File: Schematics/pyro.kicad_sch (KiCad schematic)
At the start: 6 parts, among them J6 Pyro, Q2 BSC098N10NS5

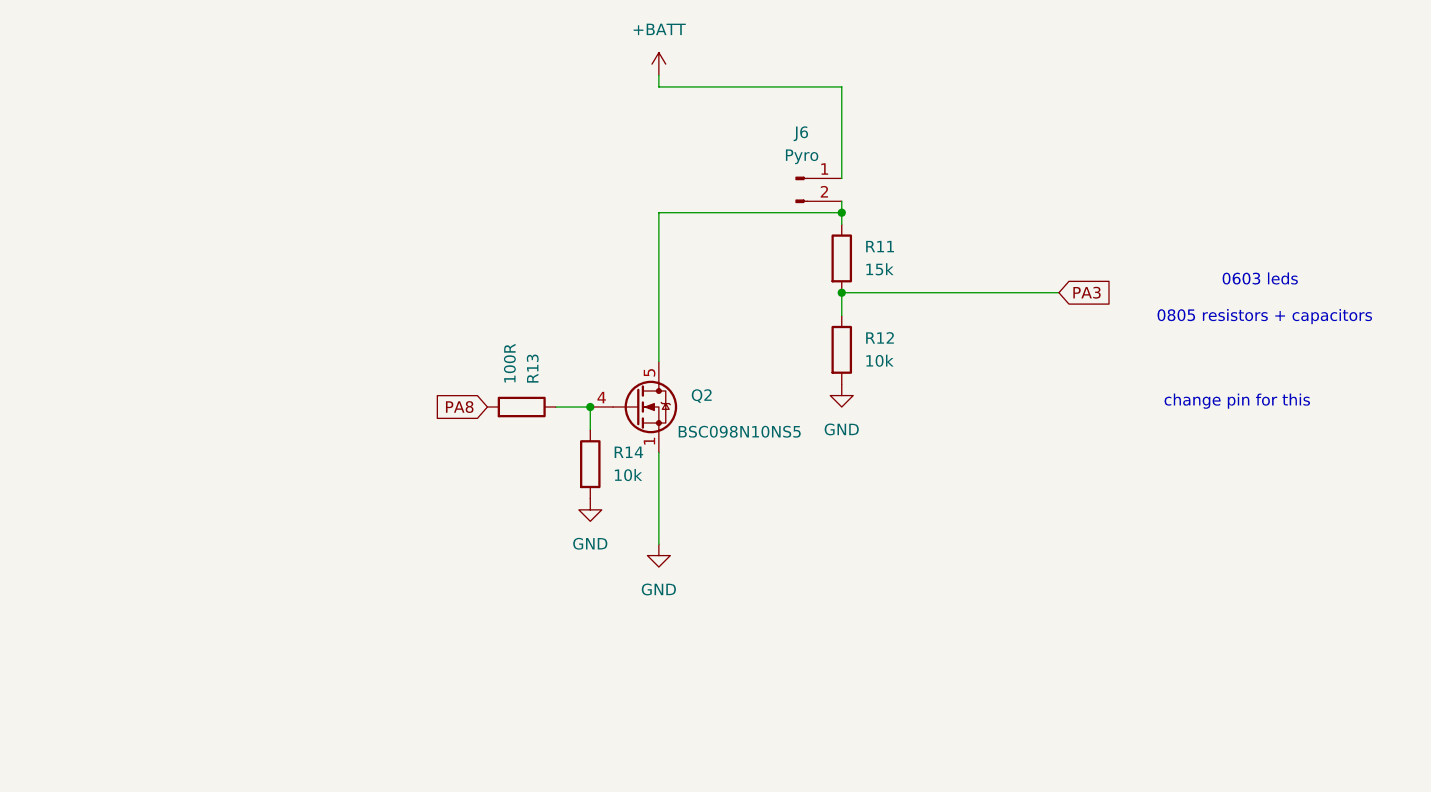
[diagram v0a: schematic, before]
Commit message: finished sensor schematics, added datasheets organized files
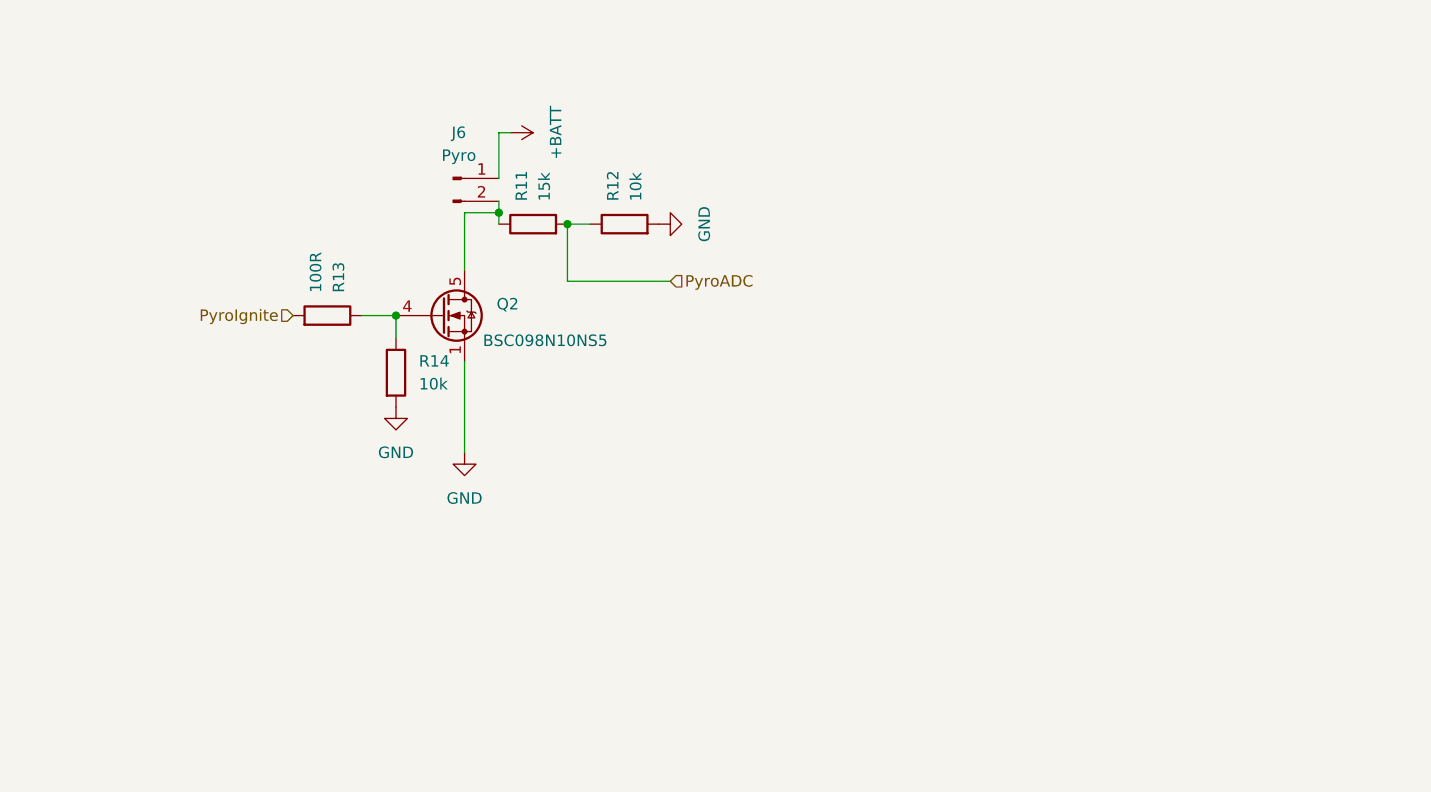
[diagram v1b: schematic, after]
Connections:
- net PA3 renamed PyroADC
- net PA8 renamed PyroIgnite
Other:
- note removed: "0603 leds"
- note removed: "0805 resistors + capacitors"
- note removed: "change pin for this"
- moved on the sheet: J6, Q2, R11, R12, R13, R14

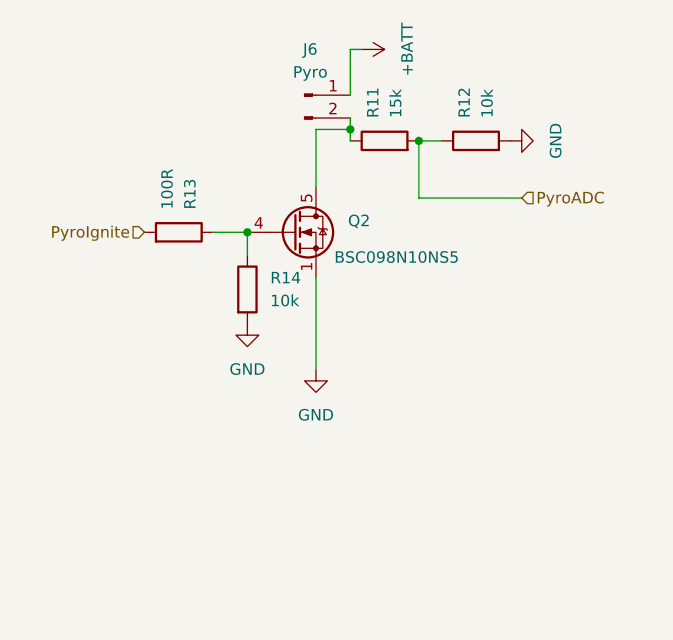
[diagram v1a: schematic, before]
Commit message: added LCSC numbers and footprint values, need to connect schemeatic pins, then can start layout
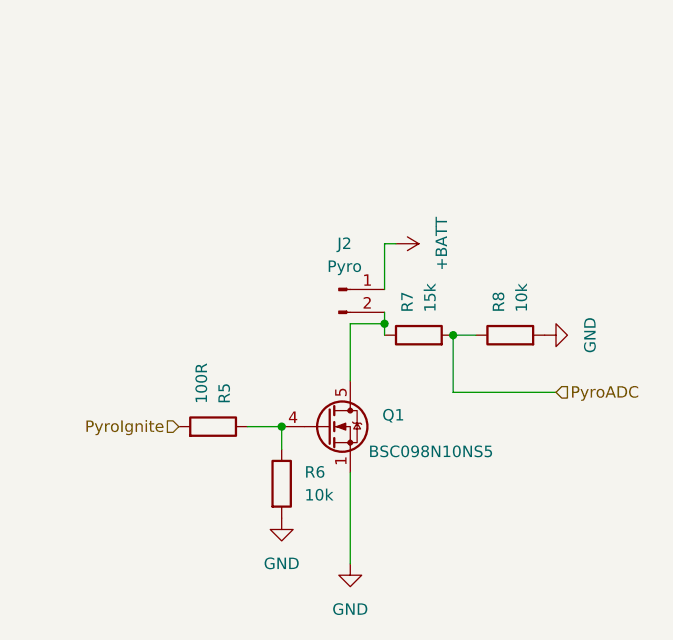
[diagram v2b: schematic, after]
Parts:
- J2: renamed from J6; footprint Connector_Molex:Molex_KK-254_AE-6410-02A_1x02_P2.54mm_Vertical -> myFootprints:MOLEX_26013114; LCSC Part (none) -> C17644051
- Q1: renamed from Q2; LCSC Part (none) -> C534398
- R5: renamed from R13; LCSC Part (none) -> C17408
- R6: renamed from R14; LCSC Part (none) -> C84376
- R7: renamed from R11; footprint Resistor_SMD:R_0805_2012Metric -> Resistor_SMD:R_0805_2012Metric_Pad1.20x1.40mm_HandSolder; LCSC Part (none) -> C2930170
- R8: renamed from R12; LCSC Part (none) -> C84376
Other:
- moved on the sheet: J2, Q1, R5, R6, R7, R8

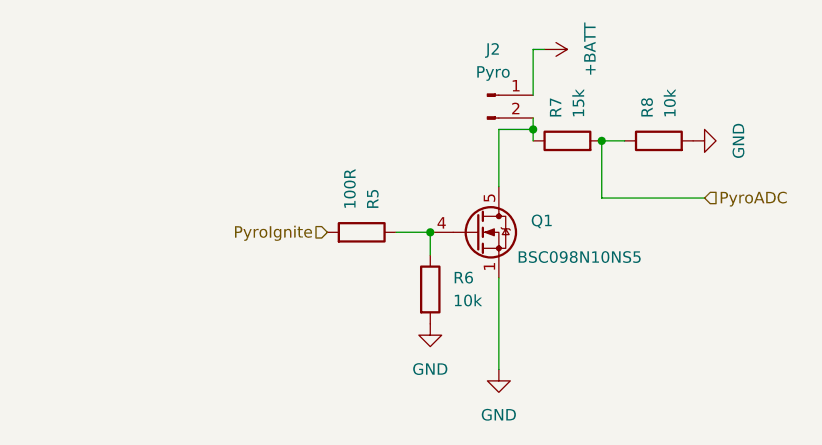
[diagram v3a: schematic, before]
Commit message: fixed symbols and added diodes to power input before ldo
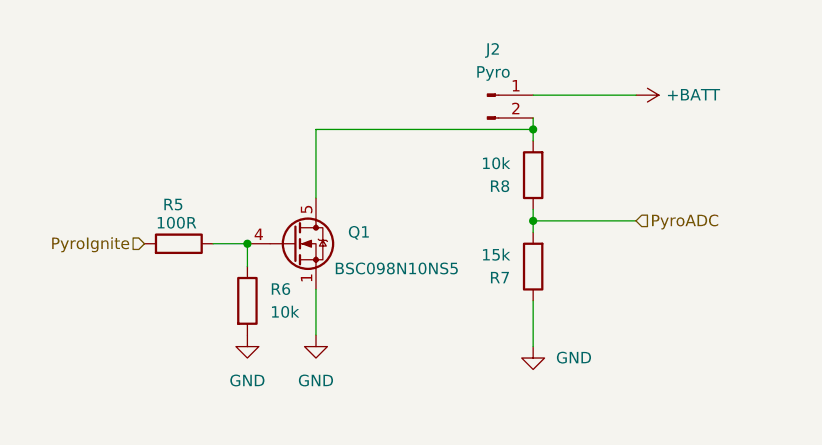
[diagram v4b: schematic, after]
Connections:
- net GND: now also R7.1; no longer R8.2
- net at J2.2 (Pin_2), Q1.5 (D): now also R8.2; no longer R7.1
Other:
- moved on the sheet: Q1, R5, R6, R7, R8

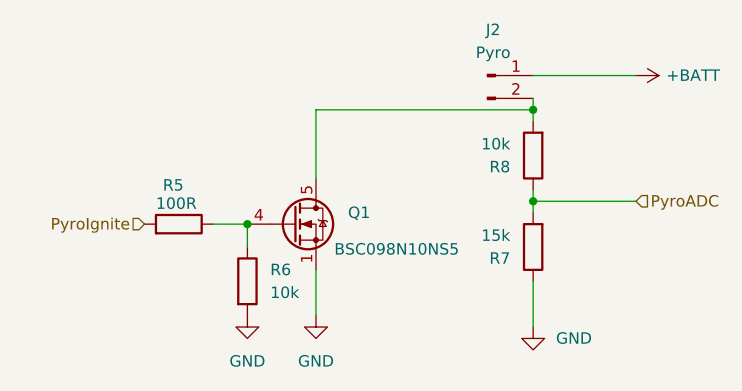
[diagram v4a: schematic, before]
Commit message: added lora correct and organizing sheet pins
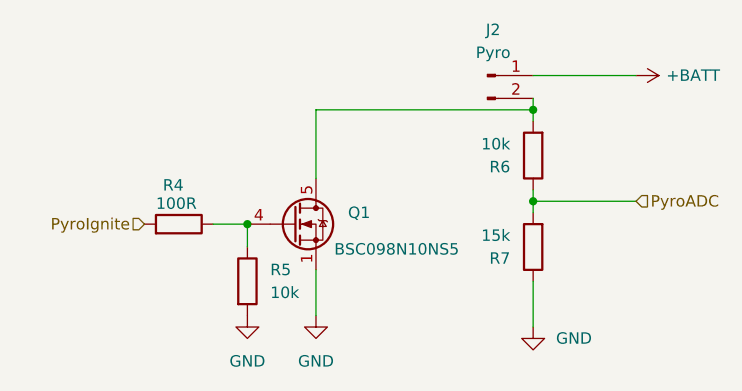
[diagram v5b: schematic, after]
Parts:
- renumbered R5 to R4, R6 to R5, R8 to R6
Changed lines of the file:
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@@
 		(dnp no)
 		(fields_autoplaced yes)
-		(property "Reference" "R8"
+		(property "Reference" "R6"
 			(at 118.11 87.6301 0)
 			(effects
@@
 			(project "flightcomputer2"
 				(path "/6cb3dda3-5fe8-4715-b831-354360aa3199/00a4b53a-09dd-45fe-9668-74427c57713f"
-					(reference "R8")
+					(reference "R6")
 					(unit 1)
 				)
@@
 		(on_board yes)
 		(dnp no)
-		(property "Reference" "#PWR035"
+		(property "Reference" "#PWR036"
 			(at 128.27 77.47 0)
 			(effects
@@
 			(project ""
 				(path "/6cb3dda3-5fe8-4715-b831-354360aa3199/00a4b53a-09dd-45fe-9668-74427c57713f"
-					(reference "#PWR035")
+					(reference "#PWR036")
 					(unit 1)
 				)
@@
 		(dnp no)
 		(fields_autoplaced yes)
-		(property "Reference" "R6"
+		(property "Reference" "R5"
 			(at 91.44 99.0599 0)
 			(effects
@@
 			(project "flightcomputer2"
 				(path "/6cb3dda3-5fe8-4715-b831-354360aa3199/00a4b53a-09dd-45fe-9668-74427c57713f"
-					(reference "R6")
+					(reference "R5")
 					(unit 1)
 				)
@@
 		(on_board yes)
 		(dnp no)
-		(property "Reference" "R5"
+		(property "Reference" "R4"
 			(at 79.502 89.662 90)
 			(effects
@@
 			(project "flightcomputer2"
 				(path "/6cb3dda3-5fe8-4715-b831-354360aa3199/00a4b53a-09dd-45fe-9668-74427c57713f"
-					(reference "R5")
+					(reference "R4")
 					(unit 1)
 				)
@@
 		(dnp no)
 		(fields_autoplaced yes)
-		(property "Reference" "#PWR036"
+		(property "Reference" "#PWR035"
 			(at 120.65 111.76 0)
 			(effects
@@
 			(project "flightcomputer2"
 				(path "/6cb3dda3-5fe8-4715-b831-354360aa3199/00a4b53a-09dd-45fe-9668-74427c57713f"
-					(reference "#PWR036")
-					(unit 1)
-				)
+					(reference "#PWR035")
+					(unit 1)
+				)

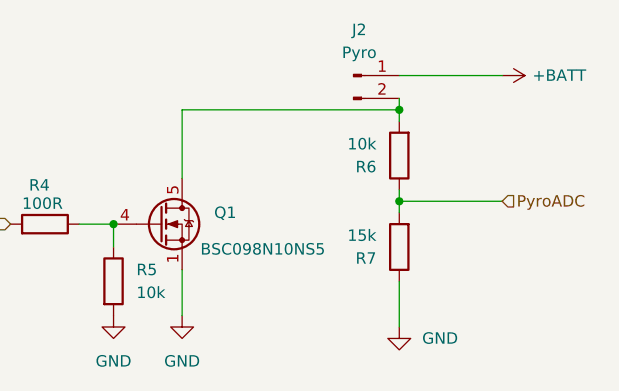
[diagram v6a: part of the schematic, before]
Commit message: first layout need to go over schematic
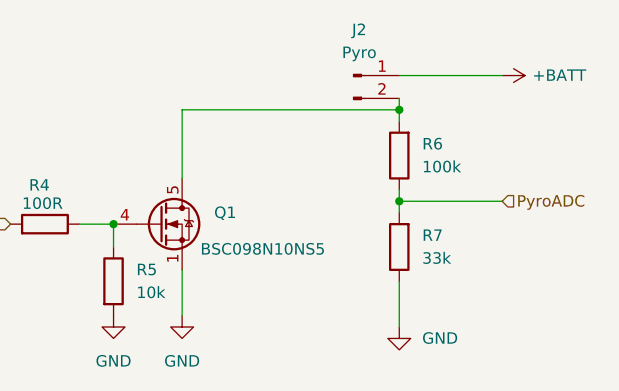
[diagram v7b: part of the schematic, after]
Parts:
- R4, R5: footprint Resistor_SMD:R_0805_2012Metric -> Resistor_SMD:R_0805_2012Metric_Pad1.20x1.40mm_HandSolder
- R6: value 10k -> 100k; footprint Resistor_SMD:R_0805_2012Metric -> Resistor_SMD:R_0805_2012Metric_Pad1.20x1.40mm_HandSolder; LCSC Part C84376 -> C96346
- R7: value 15k -> 33k; LCSC Part C2930170 -> C2933415
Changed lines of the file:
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@@
 		(fields_autoplaced yes)
 		(property "Reference" "R6"
-			(at 118.11 87.6301 0)
-			(effects
-				(font
-					(size 1.27 1.27)
-				)
-				(justify left)
-			)
-		)
-		(property "Value" "10k"
-			(at 118.11 85.0901 0)
-			(effects
-				(font
-					(size 1.27 1.27)
-				)
-				(justify left)
-			)
-		)
-		(property "Footprint" "Resistor_SMD:R_0805_2012Metric"
+			(at 123.19 85.0899 0)
+			(effects
+				(font
+					(size 1.27 1.27)
+				)
+				(justify right)
+			)
+		)
+		(property "Value" "100k"
+			(at 123.19 87.6299 0)
+			(effects
+				(font
+					(size 1.27 1.27)
+				)
+				(justify right)
+			)
+		)
+		(property "Footprint" "Resistor_SMD:R_0805_2012Metric_Pad1.20x1.40mm_HandSolder"
 			(at 122.428 86.36 90)
 			(effects
@@
 			)
 		)
-		(property "LCSC Part" "C84376"
+		(property "LCSC Part" "C96346"
 			(at 120.65 86.36 0)
 			(effects
@@
 		(fields_autoplaced yes)
 		(property "Reference" "R7"
-			(at 118.11 97.7901 0)
-			(effects
-				(font
-					(size 1.27 1.27)
-				)
-				(justify left)
-			)
-		)
-		(property "Value" "15k"
-			(at 118.11 95.2501 0)
-			(effects
-				(font
-					(size 1.27 1.27)
-				)
-				(justify left)
+			(at 123.19 95.2499 0)
+			(effects
+				(font
+					(size 1.27 1.27)
+				)
+				(justify right)
+			)
+		)
+		(property "Value" "33k"
+			(at 123.19 97.7899 0)
+			(effects
+				(font
+					(size 1.27 1.27)
+				)
+				(justify right)
 			)
 		)
@@
 			)
 		)
-		(property "LCSC Part" "C2930170"
+		(property "LCSC Part" "C2933415"
 			(at 120.65 96.52 0)
 			(effects
@@
 			)
 		)
-		(property "Footprint" "Resistor_SMD:R_0805_2012Metric"
+		(property "Footprint" "Resistor_SMD:R_0805_2012Metric_Pad1.20x1.40mm_HandSolder"
 			(at 87.122 100.33 90)
 			(effects
@@
 			)
 		)
-		(property "Footprint" "Resistor_SMD:R_0805_2012Metric"
+		(property "Footprint" "Resistor_SMD:R_0805_2012Metric_Pad1.20x1.40mm_HandSolder"
 			(at 81.28 95.758 90)
 			(effects

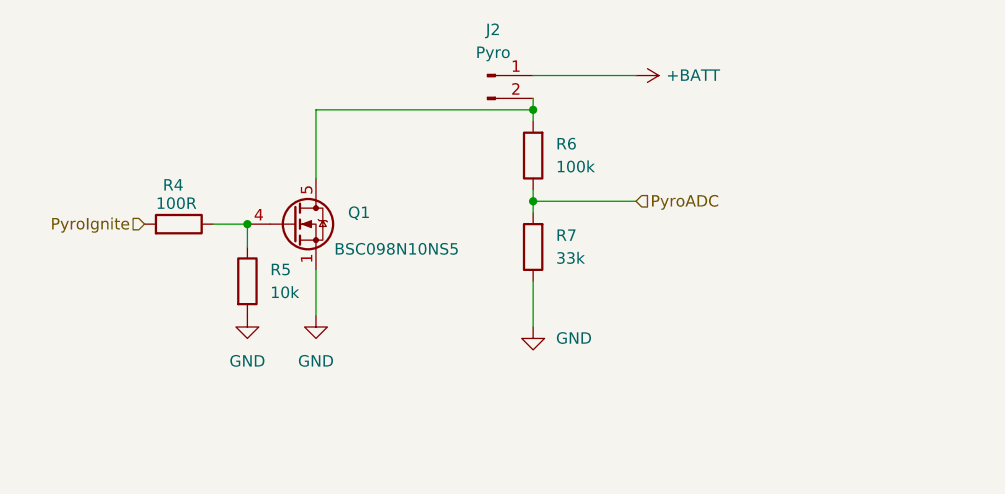
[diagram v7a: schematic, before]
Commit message: began routing, need layout approval
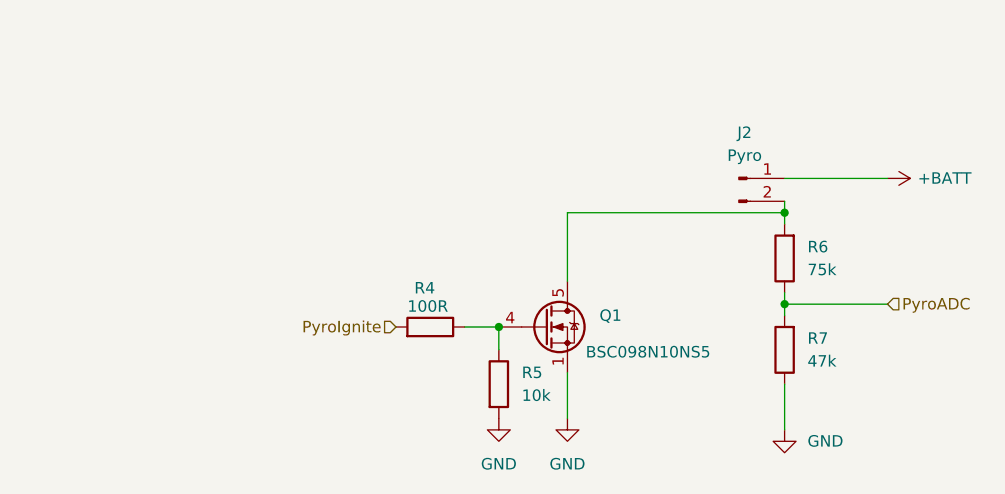
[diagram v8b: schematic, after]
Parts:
- R6: value 100k -> 75k
- R7: value 33k -> 47k
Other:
- moved on the sheet: J2, Q1, R4, R5, R6, R7
